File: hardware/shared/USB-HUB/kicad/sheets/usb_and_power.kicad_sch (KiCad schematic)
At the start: 0 parts

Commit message: feat(hardware): wire 30deg optical ring power and hub USB interfaces for accessibility pointing, ~$9 ring / ~$5-6 hub BOM
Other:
- note added: "USB/power interface scaffold: native USB pair and regulated 3V3 rail are locked here before symbol placement."
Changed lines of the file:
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@@
   (generator_version "0.1")
   (paper "A4")
+  (text "USB/power interface scaffold: native USB pair and regulated 3V3 rail are locked here before symbol placement."
+    (at 20.32 20.32 0)
+    (effects (font (size 1.27 1.27)))
+  )
+  (hierarchical_label "VREG_3V3"
+    (shape output)
+    (at 187.96 38.1 180)
+    (effects (font (size 1.27 1.27)))
+  )
+  (hierarchical_label "USB_D+"
+    (shape passive)
+    (at 187.96 45.72 180)
+    (effects (font (size 1.27 1.27)))
+  )
+  (hierarchical_label "USB_D-"
+    (shape passive)
+    (at 187.96 53.34 180)
+    (effects (font (size 1.27 1.27)))
+  )
   (sheet_instances
     (path "/" (page "1"))

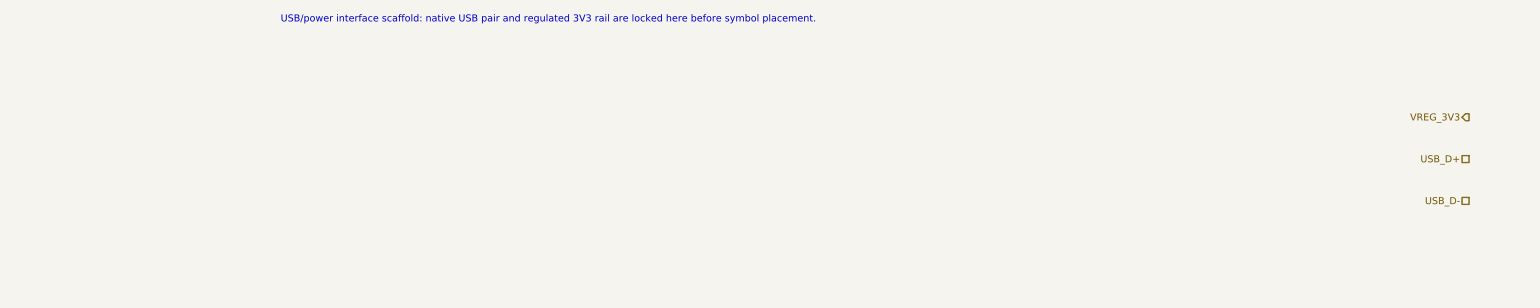
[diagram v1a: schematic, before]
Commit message: feat(hardware): capture native-USB BLE hub dongle power tree for accessibility pointing, ~$5-6 BOM
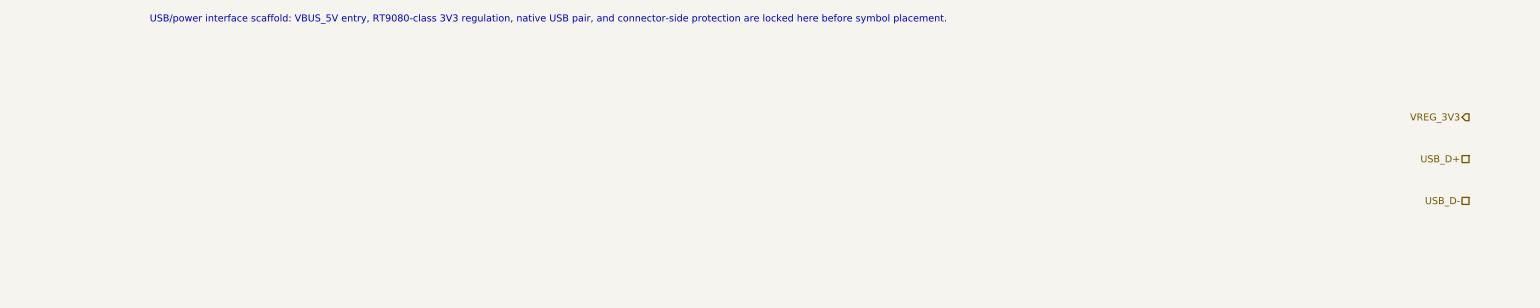
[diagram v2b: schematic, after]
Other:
- note added: "USB/power interface scaffold: VBUS_5V entry, RT9080-class 3V3 regulation, native USB pair, and connector-side protection are locked here before symbol placement."
- note removed: "USB/power interface scaffold: native USB pair and regulated 3V3 rail are locked here before symbol placement."
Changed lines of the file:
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@@
   (generator_version "0.1")
   (paper "A4")
-  (text "USB/power interface scaffold: native USB pair and regulated 3V3 rail are locked here before symbol placement."
+  (text "USB/power interface scaffold: VBUS_5V entry, RT9080-class 3V3 regulation, native USB pair, and connector-side protection are locked here before symbol placement."
     (at 20.32 20.32 0)
     (effects (font (size 1.27 1.27)))

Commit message: feat(hardware): lock native-USB BLE hub dongle first-board parts for accessibility pointing, ~$5-6 BOM
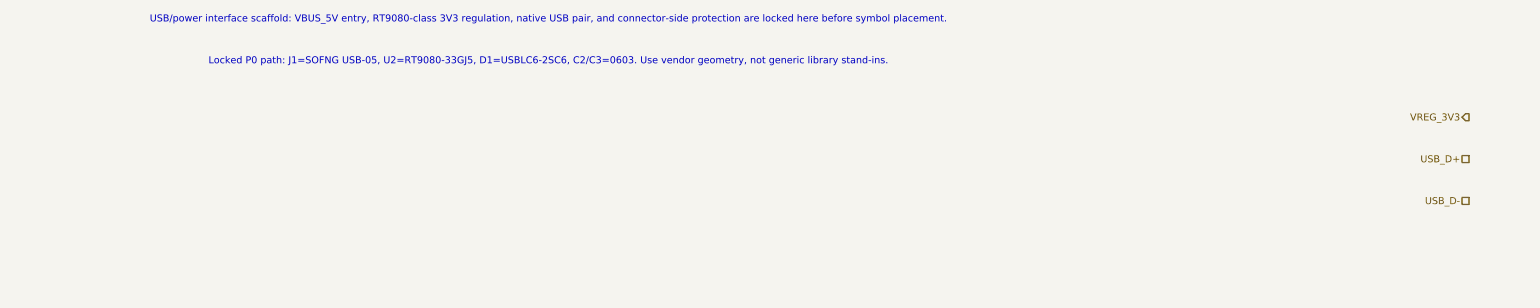
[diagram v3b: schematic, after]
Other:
- note added: "Locked P0 path: J1=SOFNG USB-05, U2=RT9080-33GJ5, D1=USBLC6-2SC6, C2/C3=0603. Use vendor geometry, not generic library stand-ins."
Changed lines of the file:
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@@
+    (effects (font (size 1.27 1.27)))
+  )
+  (text "Locked P0 path: J1=SOFNG USB-05, U2=RT9080-33GJ5, D1=USBLC6-2SC6, C2/C3=0603. Use vendor geometry, not generic library stand-ins."
+    (at 20.32 27.94 0)
     (effects (font (size 1.27 1.27)))
   )

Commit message: feat(hardware): place native-USB BLE hub dongle usb-power symbols for accessibility pointing, ~$5-6 BOM
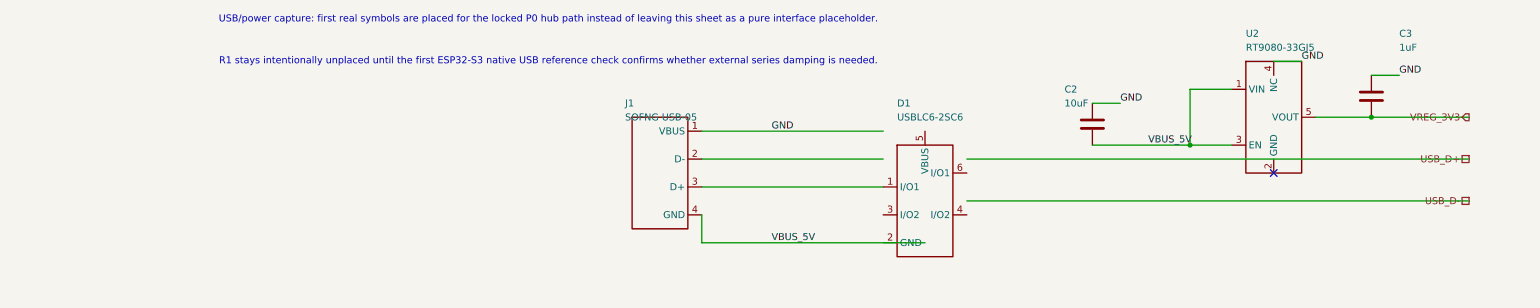
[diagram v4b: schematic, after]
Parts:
- added C2: 10uF, Capacitor_SMD:C_0603_1608Metric, symbol Device:C
- added C3: 1uF, Capacitor_SMD:C_0603_1608Metric, symbol Device:C
- added D1: USBLC6-2SC6, Package_TO_SOT_SMD:SOT-23-6, symbol PowerFinger:USBLC6-2SC6
- added J1: SOFNG USB-05, PowerFinger_USB:USB_A_Plug_SOFNG_USB-05, symbol PowerFinger:USB_A_Plug_Male
- added U2: RT9080-33GJ5, Package_TO_SOT_SMD:SOT-23-5, symbol PowerFinger:RT9080-33GJ5
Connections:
- net VREG_3V3: now also C3.2, U2.5 (VOUT)
- new net: D1.1 (I/O1), J1.3 (D+)
- new net GND: C2.1, C3.1, J1.1 (VBUS), U2.4 (NC)
- new net VBUS_5V: C2.2, J1.4 (GND), U2.1 (VIN), U2.3 (EN)
- no-connect marks 0 -> 1
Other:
- note added: "R1 stays intentionally unplaced until the first ESP32-S3 native USB reference check confirms whether external series damping is needed."
- note added: "USB/power capture: first real symbols are placed for the locked P0 hub path instead of leaving this sheet as a pure interface placeholder."
- note removed: "Locked P0 path: J1=SOFNG USB-05, U2=RT9080-33GJ5, D1=USBLC6-2SC6, C2/C3=0603. Use vendor geometry, not generic library stand-ins."
- note removed: "USB/power interface scaffold: VBUS_5V entry, RT9080-class 3V3 regulation, native USB pair, and connector-side protection are locked here before symbol placement."

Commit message: feat(usb-hub): add native usb first-board pass
Defensive publication:

- Specific sensing mechanism: no surface sensor on the hub; native USB ESP32-S3 service/programming and HID bridge capture for the PowerFinger BLE input family.

- Form factor and angle: straight inline direct-plug USB-A dongle board, first-pass 54 x 26 mm layout with reinforced SOFNG USB-05 plug retention.

- Intended use case: offline accessible first-board bring-up, repair, programming, and native-USB service for PowerFinger ring/wand development.

- BOM estimate: keeps the active USB-HUB packet inside the current ~$5-6 first-board BOM intent.

Verification:

- git diff --check -- hardware/shared/USB-HUB

- KiCad CLI ERC/DRC run locally and documented as still failing pending schematic connectivity and PCB routing closure.
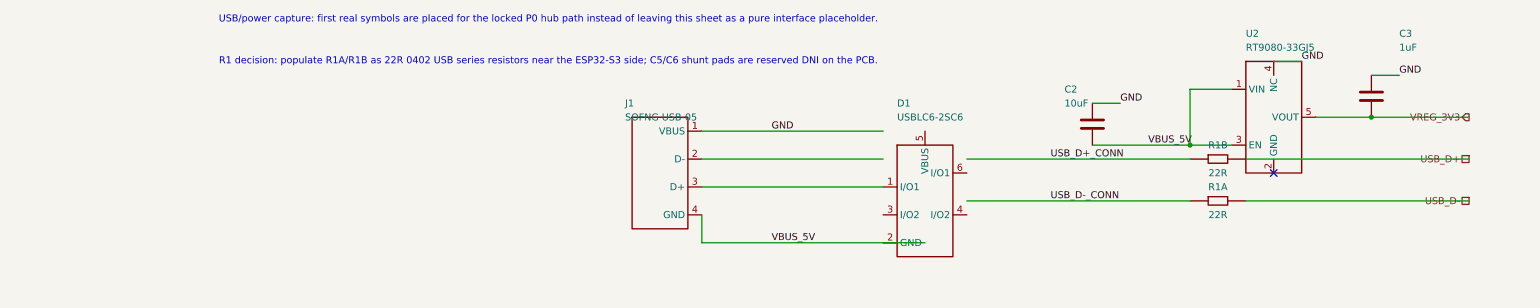
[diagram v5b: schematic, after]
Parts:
- added R1A, R1B: 22R, Resistor_SMD:R_0402_1005Metric, symbol PowerFinger:R_USB_SERIES
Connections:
- net USB_D+: now also R1B.2
- net USB_D-: now also R1A.2
- new net USB_D+_CONN: R1B.1
- new net USB_D-_CONN: R1A.1
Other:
- note added: "R1 decision: populate R1A/R1B as 22R 0402 USB series resistors near the ESP32-S3 side; C5/C6 shunt pads are reserved DNI on the PCB."
- note removed: "R1 stays intentionally unplaced until the first ESP32-S3 native USB reference check confirms whether external series damping is needed."
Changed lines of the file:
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@@
     (effects (font (size 1.27 1.27)))
   )
-  (text "R1 stays intentionally unplaced until the first ESP32-S3 native USB reference check confirms whether external series damping is needed."
+  (text "R1 decision: populate R1A/R1B as 22R 0402 USB series resistors near the ESP32-S3 side; C5/C6 shunt pads are reserved DNI on the PCB."
     (at 20.32 27.94 0)
     (effects (font (size 1.27 1.27)))
@@
   (label "GND"
     (at 175.26 30.48 0)
+    (effects (font (size 1.27 1.27)) (justify left bottom))
+  )
+  (label "USB_D+_CONN"
+    (at 111.76 45.72 0)
+    (effects (font (size 1.27 1.27)) (justify left bottom))
+  )
+  (label "USB_D-_CONN"
+    (at 111.76 53.34 0)
     (effects (font (size 1.27 1.27)) (justify left bottom))
   )
@@
     (pts
       (xy 96.52 53.34)
+      (xy 137.16 53.34)
+    )
+    (stroke (width 0) (type default) (color 0 0 0 0))
+  )
+  (wire
+    (pts
+      (xy 147.32 53.34)
       (xy 187.96 53.34)
     )
@@
     (pts
       (xy 96.52 45.72)
+      (xy 137.16 45.72)
+    )
+    (stroke (width 0) (type default) (color 0 0 0 0))
+  )
+  (wire
+    (pts
+      (xy 147.32 45.72)
       (xy 187.96 45.72)
     )
@@
         )
       )
+    )
+  )
+  (symbol (lib_id "PowerFinger:R_USB_SERIES") (at 142.24 53.34 0) (unit 1)
+    (in_bom yes) (on_board yes) (dnp no) (fields_autoplaced)
+    (property "Reference" "R1A" (at 142.24 50.8 0)
+      (effects (font (size 1.27 1.27)))
+    )
+    (property "Value" "22R" (at 142.24 55.88 0)
+      (effects (font (size 1.27 1.27)))
+    )
+    (property "Footprint" "Resistor_SMD:R_0402_1005Metric" (at 142.24 48.26 0)
+      (effects (font (size 1.27 1.27)) hide)
+    )
+    (property "Role" "USB_D- series damping near U1" (at 142.24 45.72 0)
+      (effects (font (size 1.27 1.27)) hide)
+    )
+    (pin "1")
+    (pin "2")
+    (instances
+      (project "usb_hub"
+        (path "/"
+          (reference "R1A") (unit 1)
+        )
+      )
+    )
+  )
+  (symbol (lib_id "PowerFinger:R_USB_SERIES") (at 142.24 45.72 0) (unit 1)
+    (in_bom yes) (on_board yes) (dnp no) (fields_autoplaced)
+    (property "Reference" "R1B" (at 142.24 43.18 0)
+      (effects (font (size 1.27 1.27)))
+    )
+    (property "Value" "22R" (at 142.24 48.26 0)
+      (effects (font (size 1.27 1.27)))
+    )
+    (property "Footprint" "Resistor_SMD:R_0402_1005Metric" (at 142.24 40.64 0)
+      (effects (font (size 1.27 1.27)) hide)
+    )
+    (property "Role" "USB_D+ series damping near U1" (at 142.24 38.1 0)
+      (effects (font (size 1.27 1.27)) hide)
+    )
+    (pin "1")
+    (pin "2")
+    (instances
+      (project "usb_hub"
+        (path "/"
+          (reference "R1B") (unit 1)
+        )
+      )

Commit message: feat(usb-hub): clean native USB first board pass
Sensing mechanism: none; native USB-A hub/control accessory capture for the shared USB-HUB packet.

Form factor and angle: direct-plug USB-A dongle first-board PCB; no ring angle applies.

Intended use case: offline native-USB repairable hub/control bring-up for accessibility pointing devices.

BOM estimate: kept inside the current USB-HUB approximately -6 first-board intent.
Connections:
- net GND: now also D1.2 (GND), J1.4 (GND), U2.2 (GND); no longer J1.1 (VBUS), U2.4 (NC)
- net USB_D+_CONN: now also D1.3 (I/O2), D1.4 (I/O2), J1.3 (D+)
- net USB_D-_CONN: now also D1.1 (I/O1), D1.6 (I/O1), J1.2 (D-)
- net VBUS_5V: now also D1.5 (VBUS), J1.1 (VBUS); no longer J1.4 (GND)
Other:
- note added: "R1 decision: populate R1A/R1B as 22R 0402 USB series resistors near the ESP32-S3 side; C5/C6 are no-net DNI placeholders in this clean pass."
- note removed: "R1 decision: populate R1A/R1B as 22R 0402 USB series resistors near the ESP32-S3 side; C5/C6 shunt pads are reserved DNI on the PCB."
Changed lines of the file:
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@@
     (effects (font (size 1.27 1.27)))
   )
-  (text "R1 decision: populate R1A/R1B as 22R 0402 USB series resistors near the ESP32-S3 side; C5/C6 shunt pads are reserved DNI on the PCB."
+  (text "R1 decision: populate R1A/R1B as 22R 0402 USB series resistors near the ESP32-S3 side; C5/C6 are no-net DNI placeholders in this clean pass."
     (at 20.32 27.94 0)
     (effects (font (size 1.27 1.27)))
@@
   )
   (label "VBUS_5V"
-    (at 60.96 60.96 0)
+    (at 60.96 40.64 0)
+    (effects (font (size 1.27 1.27)) (justify left bottom))
+  )
+  (label "VBUS_5V"
+    (at 96.52 40.64 0)
+    (effects (font (size 1.27 1.27)) (justify left bottom))
+  )
+  (label "VBUS_5V"
+    (at 137.16 33.02 0)
     (effects (font (size 1.27 1.27)) (justify left bottom))
   )
@@
   )
   (label "GND"
-    (at 60.96 40.64 0)
-    (effects (font (size 1.27 1.27)) (justify left bottom))
-  )
-  (label "GND"
-    (at 124.46 35.56 0)
-    (effects (font (size 1.27 1.27)) (justify left bottom))
-  )
-  (label "GND"
-    (at 157.48 27.94 0)
+    (at 60.96 55.88 0)
+    (effects (font (size 1.27 1.27)) (justify left bottom))
+  )
+  (label "GND"
+    (at 73.66 60.96 0)
+    (effects (font (size 1.27 1.27)) (justify left bottom))
+  )
+  (label "GND"
+    (at 129.54 35.56 0)
+    (effects (font (size 1.27 1.27)) (justify left bottom))
+  )
+  (label "GND"
+    (at 160.02 48.26 0)
     (effects (font (size 1.27 1.27)) (justify left bottom))
   )
@@
     (effects (font (size 1.27 1.27)) (justify left bottom))
   )
-  (label "USB_D+_CONN"
-    (at 111.76 45.72 0)
-    (effects (font (size 1.27 1.27)) (justify left bottom))
-  )
-  (label "USB_D-_CONN"
-    (at 111.76 53.34 0)
+  (label "USB_D-_CONN"
+    (at 60.96 45.72 0)
+    (effects (font (size 1.27 1.27)) (justify left bottom))
+  )
+  (label "USB_D+_CONN"
+    (at 60.96 50.8 0)
+    (effects (font (size 1.27 1.27)) (justify left bottom))
+  )
+  (label "USB_D-_CONN"
+    (at 73.66 50.8 0)
+    (effects (font (size 1.27 1.27)) (justify left bottom))
+  )
+  (label "USB_D+_CONN"
+    (at 73.66 55.88 0)
+    (effects (font (size 1.27 1.27)) (justify left bottom))
+  )
+  (label "USB_D-_CONN"
+    (at 106.68 48.26 0)
+    (effects (font (size 1.27 1.27)) (justify left bottom))
+  )
+  (label "USB_D+_CONN"
+    (at 106.68 55.88 0)
     (effects (font (size 1.27 1.27)) (justify left bottom))
   )
@@
   )
   (no_connect
-    (at 152.4 48.26)
+    (at 152.4 27.94)
+  )
+  (wire
+    (pts
+      (xy 48.26 40.64)
+      (xy 60.96 40.64)
+    )
+    (stroke (width 0) (type default) (color 0 0 0 0))
+  )
+  (wire
+    (pts
+      (xy 60.96 40.64)
+      (xy 68.58 40.64)
+    )
+    (stroke (width 0) (type default) (color 0 0 0 0))
+  )
+  (wire
+    (pts
+      (xy 48.26 45.72)
+      (xy 60.96 45.72)
+    )
+    (stroke (width 0) (type default) (color 0 0 0 0))
+  )
+  (wire
+    (pts
+      (xy 48.26 50.8)
+      (xy 60.96 50.8)
+    )
+    (stroke (width 0) (type default) (color 0 0 0 0))
   )
   (wire
     (pts
       (xy 48.26 55.88)
-      (xy 48.26 60.96)
-    )
-    (stroke (width 0) (type default) (color 0 0 0 0))
-  )
-  (wire
-    (pts
-      (xy 48.26 60.96)
-      (xy 88.9 60.96)
-    )
-    (stroke (width 0) (type default) (color 0 0 0 0))
-  )
-  (wire
-    (pts
-      (xy 48.26 50.8)
+      (xy 60.96 55.88)
+    )
+    (stroke (width 0) (type default) (color 0 0 0 0))
+  )
+  (wire
+    (pts
+      (xy 60.96 55.88)
+      (xy 68.58 55.88)
+    )
+    (stroke (width 0) (type default) (color 0 0 0 0))
+  )
+  (wire
+    (pts
       (xy 81.28 50.8)
-    )
-    (stroke (width 0) (type default) (color 0 0 0 0))
-  )
-  (wire
-    (pts
-      (xy 48.26 45.72)
-      (xy 81.28 45.72)
-    )
-    (stroke (width 0) (type default) (color 0 0 0 0))
-  )
-  (wire
-    (pts
-      (xy 48.26 40.64)
-      (xy 81.28 40.64)
-    )
-    (stroke (width 0) (type default) (color 0 0 0 0))
-  )
-  (wire
-    (pts
-      (xy 96.52 53.34)
+      (xy 73.66 50.8)
+    )
+    (stroke (width 0) (type default) (color 0 0 0 0))
+  )
+  (wire
+    (pts
+      (xy 81.28 55.88)
+      (xy 73.66 55.88)
+    )
+    (stroke (width 0) (type default) (color 0 0 0 0))
+  )
+  (wire
+    (pts
+      (xy 81.28 60.96)
+      (xy 73.66 60.96)
+    )
+    (stroke (width 0) (type default) (color 0 0 0 0))
+  )
+  (wire
+    (pts
+      (xy 88.9 40.64)
+      (xy 96.52 40.64)
+    )
+    (stroke (width 0) (type default) (color 0 0 0 0))
+  )
+  (wire
+    (pts
+      (xy 96.52 48.26)
+      (xy 106.68 48.26)
+    )
+    (stroke (width 0) (type default) (color 0 0 0 0))
+  )
+  (wire
+    (pts
+      (xy 96.52 55.88)
+      (xy 106.68 55.88)
+    )
+    (stroke (width 0) (type default) (color 0 0 0 0))
+  )
+  (wire
+    (pts
       (xy 137.16 53.34)
-    )
-    (stroke (width 0) (type default) (color 0 0 0 0))
+      (xy 129.54 53.34)
+    )
+    (stroke (width 0) (type default) (color 0 0 0 0))
+  )
+  (label "USB_D-_CONN"
+    (at 129.54 53.34 0)
+    (effects (font (size 1.27 1.27)) (justify left bottom))
   )
   (wire
@@
   (wire
     (pts
-      (xy 96.52 45.72)
       (xy 137.16 45.72)
-    )
-    (stroke (width 0) (type default) (color 0 0 0 0))
+      (xy 129.54 45.72)
+    )
+    (stroke (width 0) (type default) (color 0 0 0 0))
+  )
+  (label "USB_D+_CONN"
+    (at 129.54 45.72 0)
+    (effects (font (size 1.27 1.27)) (justify left bottom))
   )
   (wire
@@
   (wire
     (pts
+      (xy 144.78 33.02)
+      (xy 137.16 33.02)
+    )
+    (stroke (width 0) (type default) (color 0 0 0 0))
+  )
+  (wire
+    (pts
+      (xy 144.78 43.18)
+      (xy 129.54 43.18)
+    )
+    (stroke (width 0) (type default) (color 0 0 0 0))
+  )
+  (wire
+    (pts
+      (xy 119.38 35.56)
+      (xy 129.54 35.56)
+    )
+    (stroke (width 0) (type default) (color 0 0 0 0))
+  )
+  (wire
+    (pts
       (xy 119.38 43.18)
-      (xy 144.78 43.18)
-    )
-    (stroke (width 0) (type default) (color 0 0 0 0))
-  )
-  (wire
-    (pts
-      (xy 137.16 43.18)
-      (xy 137.16 33.02)
-    )
-    (stroke (width 0) (type default) (color 0 0 0 0))
-  )
-  (wire
-    (pts
-      (xy 137.16 33.02)
-      (xy 144.78 33.02)
-    )
-    (stroke (width 0) (type default) (color 0 0 0 0))
-  )
-  (wire
-    (pts
-      (xy 119.38 35.56)
-      (xy 124.46 35.56)
-    )
-    (stroke (width 0) (type default) (color 0 0 0 0))
-  )
-  (wire
-    (pts
-      (xy 152.4 27.94)
-      (xy 157.48 27.94)
+      (xy 129.54 43.18)
+    )
+    (stroke (width 0) (type default) (color 0 0 0 0))
+  )
+  (wire
+    (pts
+      (xy 152.4 48.26)
+      (xy 160.02 48.26)
     )
     (stroke (width 0) (type default) (color 0 0 0 0))
@@
     (pts
       (xy 160.02 38.1)
-      (xy 170.18 38.1)
-    )
-    (stroke (width 0) (type default) (color 0 0 0 0))
-  )
-  (wire
-    (pts
-      (xy 170.18 38.1)
       (xy 187.96 38.1)
     )
@@
     (stroke (width 0) (type default) (color 0 0 0 0))
   )
+  (symbol (lib_id "power:PWR_FLAG") (at 68.58 40.64 0) (unit 1)
+    (in_bom no) (on_board no) (dnp no)
+    (property "Reference" "#FLG0101" (at 68.58 38.735 0)
+      (effects (font (size 1.27 1.27)) hide)
+    )
+    (property "Value" "PWR_FLAG" (at 68.58 36.83 0)
+      (effects (font (size 1.27 1.27)))
+    )
+    (pin "1")
+    (instances
+      (project "usb_hub"
+        (path "/"
+          (reference "#FLG0101") (unit 1)
+        )
+      )
+    )
+  )
+  (symbol (lib_id "power:PWR_FLAG") (at 68.58 55.88 0) (unit 1)
+    (in_bom no) (on_board no) (dnp no)
+    (property "Reference" "#FLG0102" (at 68.58 53.975 0)
+      (effects (font (size 1.27 1.27)) hide)
+    )
+    (property "Value" "PWR_FLAG" (at 68.58 52.07 0)
+      (effects (font (size 1.27 1.27)))
+    )
+    (pin "1")
+    (instances
+      (project "usb_hub"
+        (path "/"
+          (reference "#FLG0102") (unit 1)
+        )
+      )
+    )
+  )
   (symbol (lib_id "PowerFinger:USB_A_Plug_Male") (at 40.64 48.26 0) (unit 1)
